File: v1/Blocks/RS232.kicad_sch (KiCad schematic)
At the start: 8 parts, among them IC31 MAX3221IDBRE4, J10 Conn_02x01, J8 750678-1, J9 Conn_02x01

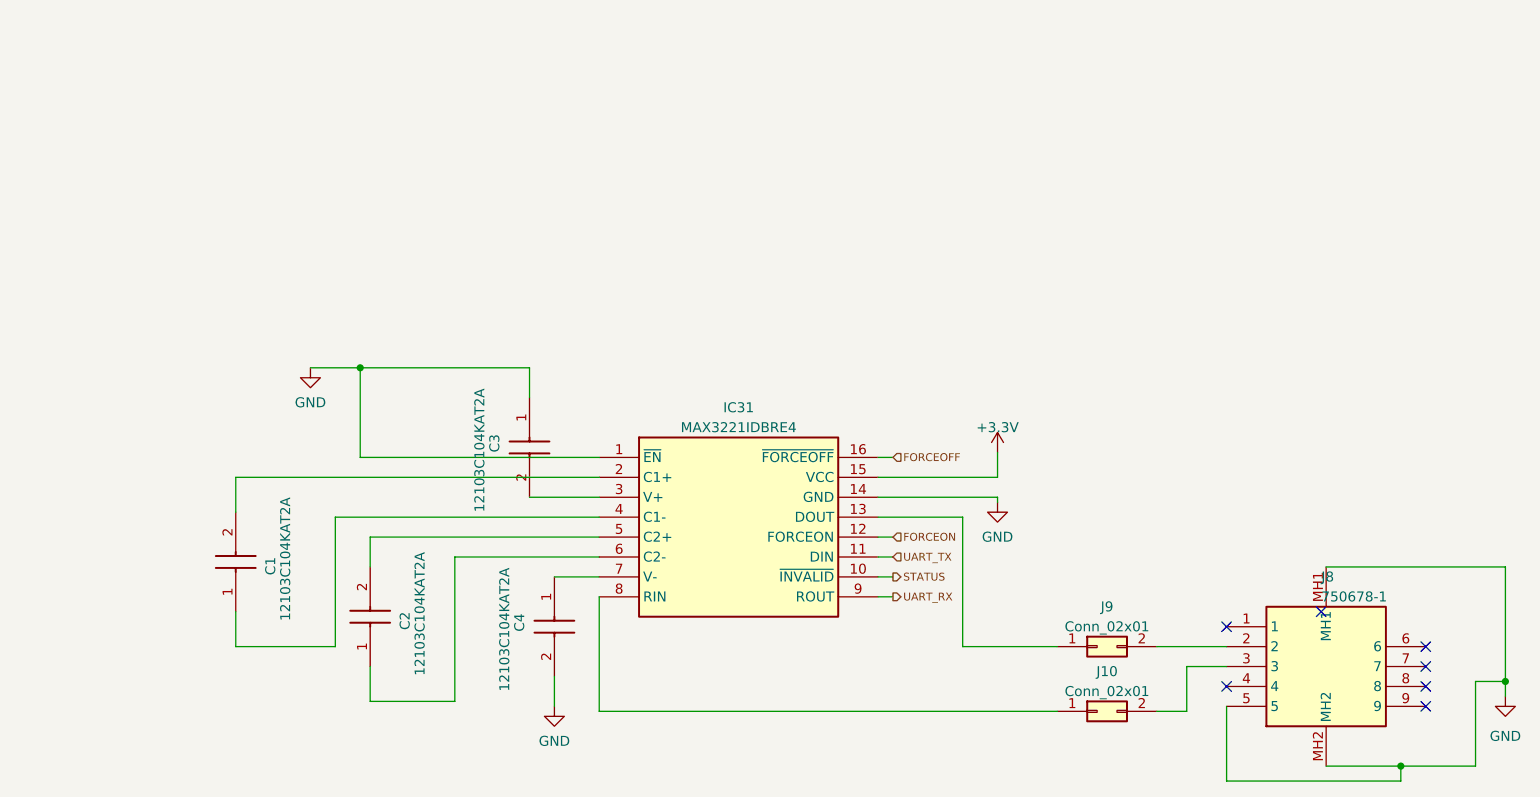
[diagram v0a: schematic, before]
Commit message: Update views, to make drawing sheets smaller where necessary
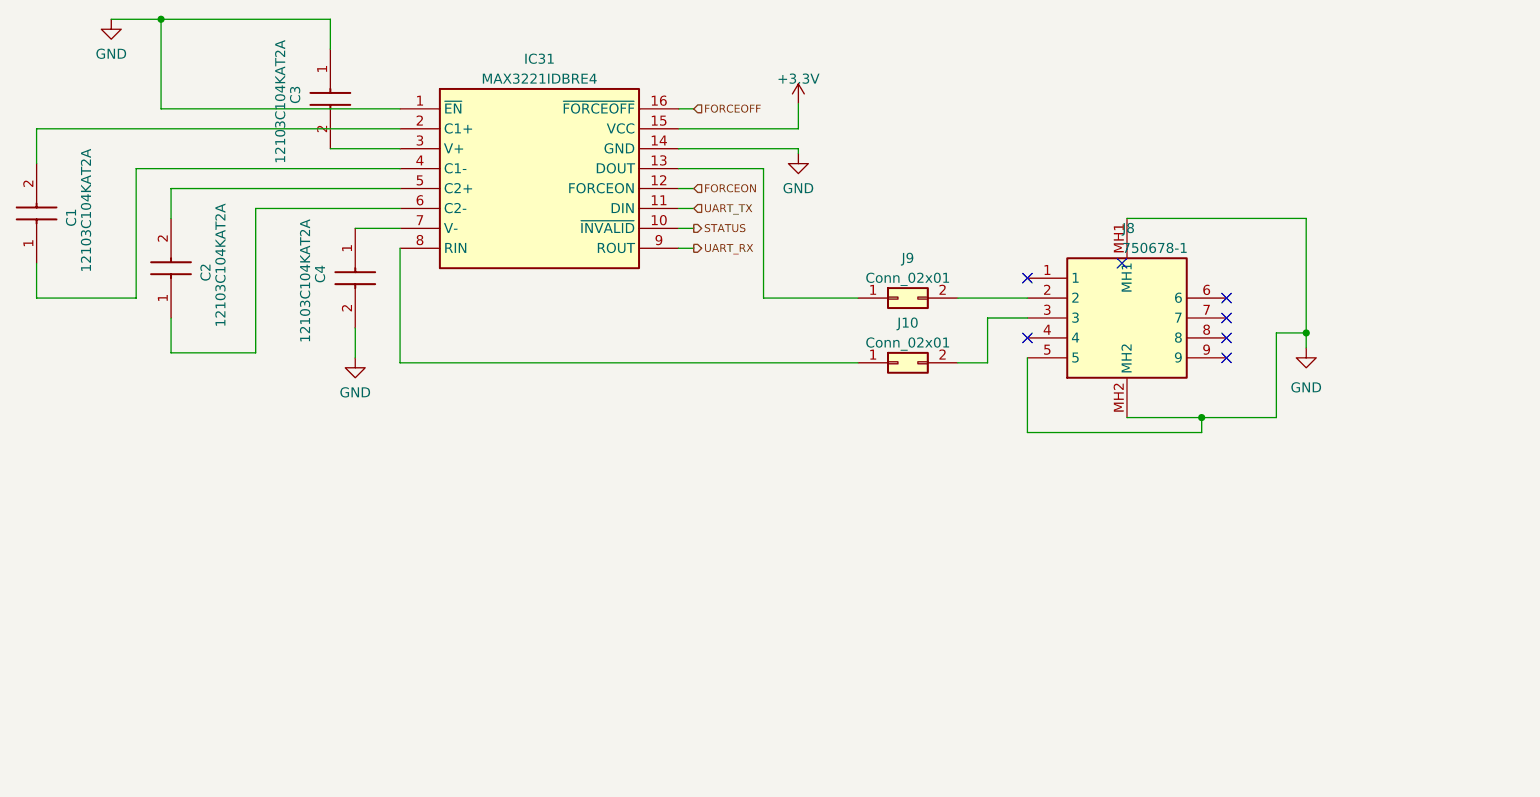
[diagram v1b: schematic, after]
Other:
- moved on the sheet: C1, C2, C3, C4, IC31, J10, J8, J9
